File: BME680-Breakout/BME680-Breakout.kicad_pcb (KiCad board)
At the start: 2 copper layers, 15.7 x 10.7 mm, 3 parts, among them J1 LeftPins, J2 RightPins, U1 BME680

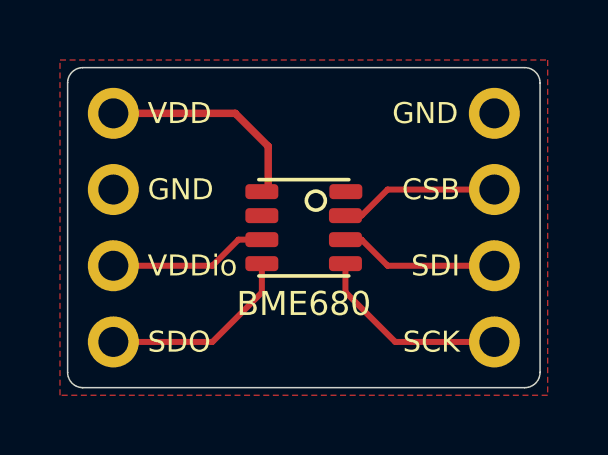
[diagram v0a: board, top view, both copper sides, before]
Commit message: use a BME680 footprint with much larger solder pads for greatier happiness
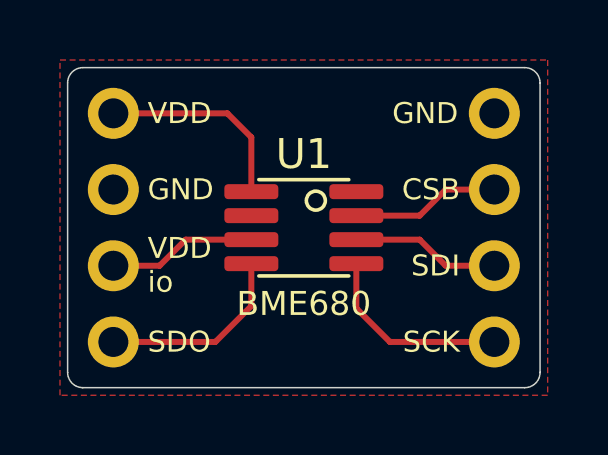
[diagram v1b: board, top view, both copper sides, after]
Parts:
- U1: footprint BME680-Breakout:Bosch_LGA-8_3x3mm_P0.8mm_ClockwisePinNumbering -> GlobalParts:Bosch_LGA-8_3x3mm_P0.8mm_ClockwisePinNumbering_LargePads
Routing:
- net Net-(J2-Pad3): track 5.52 -> 4.96 mm
- net Net-(J2-Pad2): track 5.52 -> 4.96 mm
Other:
- board text added: "BME680 Breakout rev02 xrstf.de CC BY-SA 4.0"
- board text added: "VDD io"
- board text removed: "BME680 Breakout rev01 xrstf.de CC BY-SA 4.0"
- board text removed: "VDDio"
